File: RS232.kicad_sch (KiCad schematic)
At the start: 5 parts, among them U5 MAX3221

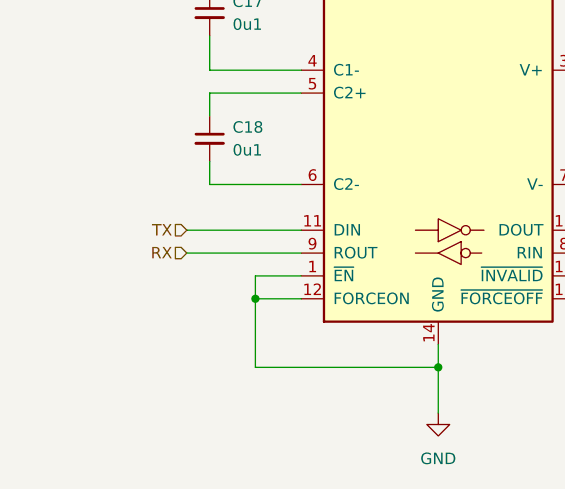
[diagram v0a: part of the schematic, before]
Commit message: Swapped USART1 RX/TX, added pull ups for USART lines
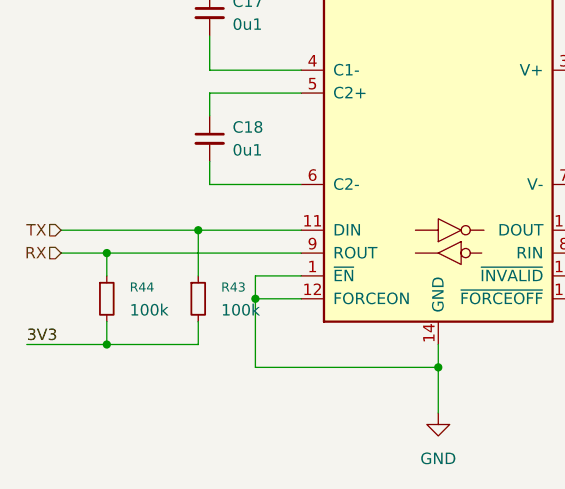
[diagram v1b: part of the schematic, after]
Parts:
- added R43, R44: 100k, Resistor_SMD:R_0603_1608Metric_Pad0.98x0.95mm_HandSolder, symbol Device:R_Small
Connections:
- net 3V3: now also R43.2, R44.2
- net RX: now also R44.1
- net TX: now also R43.1
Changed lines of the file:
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@@
 	(paper "A4")
+	(junction
+		(at 105.41 105.41)
+		(diameter 0)
+		(color 0 0 0 0)
+	)
 	(junction
 		(at 121.92 110.49)
@@
 		(color 0 0 0 0)
 	)
+	(junction
+		(at 115.57 102.87)
+		(diameter 0)
+		(color 0 0 0 0)
+	)
+	(junction
+		(at 105.41 115.57)
+		(diameter 0)
+		(color 0 0 0 0)
+	)
 	(no_connect
 		(at 157.48 107.95)
@@
 	(wire
 		(pts
+			(xy 105.41 105.41) (xy 127 105.41)
+		)
+		(stroke
+			(width 0)
+			(type default)
+		)
+	)
+	(wire
+		(pts
 			(xy 185.42 104.14) (xy 185.42 109.22)
 		)
@@
 	(wire
 		(pts
+			(xy 105.41 115.57) (xy 115.57 115.57)
+		)
+		(stroke
+			(width 0)
+			(type default)
+		)
+	)
+	(wire
+		(pts
+			(xy 105.41 113.03) (xy 105.41 115.57)
+		)
+		(stroke
+			(width 0)
+			(type default)
+		)
+	)
+	(wire
+		(pts
+			(xy 115.57 102.87) (xy 115.57 107.95)
+		)
+		(stroke
+			(width 0)
+			(type default)
+		)
+	)
+	(wire
+		(pts
+			(xy 100.33 105.41) (xy 105.41 105.41)
+		)
+		(stroke
+			(width 0)
+			(type default)
+		)
+	)
+	(wire
+		(pts
 			(xy 121.92 110.49) (xy 121.92 118.11)
 		)
@@
 	(wire
 		(pts
+			(xy 115.57 102.87) (xy 127 102.87)
+		)
+		(stroke
+			(width 0)
+			(type default)
+		)
+	)
+	(wire
+		(pts
 			(xy 116.84 95.25) (xy 116.84 97.79)
 		)
@@
 	(wire
 		(pts
-			(xy 114.3 102.87) (xy 127 102.87)
-		)
-		(stroke
-			(width 0)
-			(type default)
-		)
-	)
-	(wire
-		(pts
 			(xy 157.48 102.87) (xy 166.37 102.87)
 		)
@@
 	(wire
 		(pts
+			(xy 100.33 102.87) (xy 115.57 102.87)
+		)
+		(stroke
+			(width 0)
+			(type default)
+		)
+	)
+	(wire
+		(pts
+			(xy 115.57 113.03) (xy 115.57 115.57)
+		)
+		(stroke
+			(width 0)
+			(type default)
+		)
+	)
+	(wire
+		(pts
 			(xy 127 107.95) (xy 121.92 107.95)
 		)
@@
 	(wire
 		(pts
+			(xy 105.41 105.41) (xy 105.41 107.95)
+		)
+		(stroke
+			(width 0)
+			(type default)
+		)
+	)
+	(wire
+		(pts
 			(xy 127 97.79) (xy 116.84 97.79)
 		)
@@
 	(wire
 		(pts
+			(xy 96.52 115.57) (xy 105.41 115.57)
+		)
+		(stroke
+			(width 0)
+			(type default)
+		)
+	)
+	(wire
+		(pts
 			(xy 157.48 97.79) (xy 185.42 97.79)
 		)
@@
 		)
 	)
-	(wire
-		(pts
-			(xy 114.3 105.41) (xy 127 105.41)
-		)
-		(stroke
-			(width 0)
-			(type default)
+	(label "3V3"
+		(at 96.52 115.57 0)
+		(effects
+			(font
+				(size 1.27 1.27)
+			)
+			(justify left bottom)
 		)
 	)
 	(hierarchical_label "RX"
 		(shape input)
-		(at 114.3 105.41 180)
+		(at 100.33 105.41 180)
 		(effects
 			(font
@@
 	(hierarchical_label "TX"
 		(shape input)
-		(at 114.3 102.87 180)
+		(at 100.33 102.87 180)
 		(effects
 			(font
@@
 	)
 	(symbol
+		(lib_id "Device:R_Small")
+		(at 105.41 110.49 0)
+		(unit 1)
+		(exclude_from_sim no)
+		(in_bom yes)
+		(on_board yes)
+		(dnp no)
+		(fields_autoplaced yes)
+		(property "Reference" "R44"
+			(at 107.95 109.2199 0)
+			(effects
+				(font
+					(size 1.016 1.016)
+				)
+				(justify left)
+			)
+		)
+		(property "Value" "100k"
+			(at 107.95 111.7599 0)
+			(effects
+				(font
+					(size 1.27 1.27)
+				)
+				(justify left)
+			)
+		)
+		(property "Footprint" "Resistor_SMD:R_0603_1608Metric_Pad0.98x0.95mm_HandSolder"
+			(at 105.41 110.49 0)
+			(effects
+				(font
+					(size 1.27 1.27)
+				)
+				(hide yes)
+			)
+		)
+		(property "Datasheet" "~"
+			(at 105.41 110.49 0)
+			(effects
+				(font
+					(size 1.27 1.27)
+				)
+				(hide yes)
+			)
+		)
+		(property "Description" "Resistor, small symbol"
+			(at 105.41 110.49 0)
+			(effects
+				(font
+					(size 1.27 1.27)
+				)
+				(hide yes)
+			)
+		)
+		(pin "2"
+		)
+		(pin "1"
+		)
+		(instances
+			(project "ZoneECU"
+				(path "/a97e31d4-c2fe-45e4-b8ed-feabbb54f80e/ebe4aad4-f48f-4cc0-9871-67b700b5f466"
+					(reference "R44")
+					(unit 1)
+				)
+			)
+		)
+	)
+	(symbol
 		(lib_id "Interface_UART:MAX3221")
 		(at 142.24 92.71 0)
@@
 					(unit 1)
 				)
+			)
+		)
+	)
+	(symbol
+		(lib_id "Device:R_Small")
+		(at 115.57 110.49 0)
+		(unit 1)
+		(exclude_from_sim no)
+		(in_bom yes)
+		(on_board yes)
+		(dnp no)
+		(fields_autoplaced yes)
+		(property "Reference" "R43"
+			(at 118.11 109.2199 0)
+			(effects
+				(font
+					(size 1.016 1.016)
+				)
+				(justify left)
+			)
+		)
+		(property "Value" "100k"
+			(at 118.11 111.7599 0)
+			(effects
+				(font
+					(size 1.27 1.27)
+				)
+				(justify left)
+			)
+		)
+		(property "Footprint" "Resistor_SMD:R_0603_1608Metric_Pad0.98x0.95mm_HandSolder"
+			(at 115.57 110.49 0)
+			(effects
+				(font
+					(size 1.27 1.27)
+				)
+				(hide yes)
+			)
+		)
+		(property "Datasheet" "~"
+			(at 115.57 110.49 0)
+			(effects
+				(font
+					(size 1.27 1.27)
+				)
+				(hide yes)
+			)
+		)
+		(property "Description" "Resistor, small symbol"
+			(at 115.57 110.49 0)
+			(effects
+				(font
+					(size 1.27 1.27)
+				)
+				(hide yes)
+			)
+		)
+		(pin "2"
+		)
+		(pin "1"
+		)
+		(instances
+			(project ""
+				(path "/a97e31d4-c2fe-45e4-b8ed-feabbb54f80e/ebe4aad4-f48f-4cc0-9871-67b700b5f466"
+					(reference "R43")
+					(unit 1)
+				)
